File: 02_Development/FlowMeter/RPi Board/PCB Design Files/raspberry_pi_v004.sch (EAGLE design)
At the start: 116 parts, among them J5 POWER_JACK, P1 SPL006-007, P2 SPL006-007, P3 SPL006-007, P4 SPL006-007, P5 SPL006-007, Q1 4.3A/20V/54mΩ, Q2 500mA/300V, U6 TCA9548APWR, U7 TCA9548APWR

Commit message: updated PCB with new 5V regulator (#145)
* added new 5V regulator

added new 5V regulator as existing regulator was out-of-stock at JLCPCB

* updated capacitor

changed C22 and C25 to 1206 footprint and specified 2mohm low ESR cap
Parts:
- removed C13: 33n, SparkFun-Capacitors:CAP-0805
- removed C23: 1uF, SparkFun-Capacitors:CAP-0805
- removed D3: 3A/40V/500mV, SparkFun-DiscreteSemi:DIODE-SCHOTTKY-B340A
- removed L1: INDUCTOR12.5, th_libraries:INDUCTOR12.5
- removed R1: 10K, SparkFun-Resistors:0.3OHM-0805-1/8W-1%
- removed R2: 3.3K, SparkFun-Resistors:0.3OHM-0805-1/8W-1%
- removed VREG1: XL4015, th_libraries:XL4015
- added C24: 100nF, SparkFun-Capacitors:CAP-0805
- added C25: 22uF, microbuilder:CAP_CERAMIC_1206
- added C27: 10uF, microbuilder:CAP_CERAMIC0805-NOOUTLINE
- added C28: 470nF, SparkFun-Capacitors:CAP-0805
- added C29: 4.7pF, SparkFun-Capacitors:CAP-0603
- added INDUCT: INDUCTOR_6.6_7.3, th_libraries:INDUCTOR_6.6_7.3
- added R49: 365K, SparkFun-Passives:RESISTOR0805-RES
- added R50: 49.9K, SparkFun-Passives:RESISTOR0805-RES
- added R51: 100K, SparkFun-Passives:RESISTOR0805-RES
- added R52: 10K, SparkFun-Resistors:0.3OHM-0805-1/8W-1%
- added TPS: TPS56528, th_libraries:TPS56528
- C19: value 1uF -> 10uF; device SparkFun-Capacitors:CAP-0805 -> microbuilder:CAP_CERAMIC0805-NOOUTLINE
- C20: value 1uF -> 100nF
- C22: value 220uF -> 22uF; device SparkFun-Capacitors:560UF-PANASONIC_G-25V-20% -> microbuilder:CAP_CERAMIC_1206
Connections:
- new net N$14: C24.1, TPS.VBST
- new net N$17: R51.1, TPS.PG
- new net N$27: R52.2, TPS.EN
- net 12V: now also C21.+, C27.1, R52.1, TPS.VIN; no longer C22.+, VREG1.IN
- net 5V: now also C22.1, C25.1, C29.1, INDUCT.2, R49.2; no longer C13.1, C21.+, C23.1, L1.1, R1.1
- net GND: now also C19.2, C22.2, C25.2, C27.2, C28.2, R50.2, TPS.GND, TPS.PWPD; no longer C22.-, C23.2, D3.A, R2.2, VREG1.GND
- net N$11: now also C29.2, R49.1, R50.1, TPS.VFB; no longer C13.2, R1.2, R2.1, VREG1.FB
- net N$6: now also C24.2, INDUCT.1, TPS.SW; no longer D3.C, L1.2, VREG1.SW
- net N$7: now also C28.1, R51.2, TPS.VREG; no longer C19.2, VREG1.VC
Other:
- note added: "3.3uH"
- note added: "Regulator - TPS56528DDAR https://datasheet.lcsc.com/szlcsc/1805310826_Texas-Instruments-TPS56528DDAR_C138716.pdf LCSC Part# C138716 Package SOIC - 150mill grounding pad Input Capacitor 330uF, 35V (only 25V required) LCSC Part# C134522 https://datasheet.lcsc.com/szlcsc/Lelon-VZH331M1VTR-1010K_C134522.pdf 10X10MM ROHS, panasonic G Inductor 3.3uH, 6.5amps MHCI06030-3R3M-R8A - 6.6x7.3mm LCSC Part# C2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"
- note added: "version 004 12/5/2020 - add new 5V regulator version 003 - removed piezo buzzer - used transistor/P-ch mosfet for triggering sensirion power - added 33nF capacitor on the 5V power regulator based on rev1.6 of the data sheet"
- note removed: "Regulator - XL4015E1 https://lcsc.com/product-detail/DC-DC-Converters_XL4015E1_C51661.html/?href=jlc-SMT LCSC Part# C51661 Package TO-263-5 Input capacitor Spec - 50V Selection 220uF, 50V LCSC Part# C134732 https://datasheet.lcsc.com/szlcsc/Lelon-VE-221M1HTR-1010_C134732.pdf 10X10MM ROHS, panasonic G Output Capacitor 330uF, 35V (only 25V required) LCSC Part# C134522 https://datasheet.lcsc.com/szl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"
- note removed: "version 003 - removed piezo buzzer - used transistor/P-ch mosfet for triggering sensirion power - added 33nF capacitor on the 5V power regulator based on rev1.6 of the data sheet"
- moved on the sheet: C19, C20, C21

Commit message: Next revision of PCB
Changed I2C pullup resistors to 3Kohm

General tidy up and fix of issues on the PCB. Tweaked some polygons to eliminate sharp corners, made some traces larger.
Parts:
- R10, R13, R14, R15, R16, R17, R18, R29, R30, R31, R32, R33, R34, R35, R36, R7, R8, R9: value 10K -> 3K

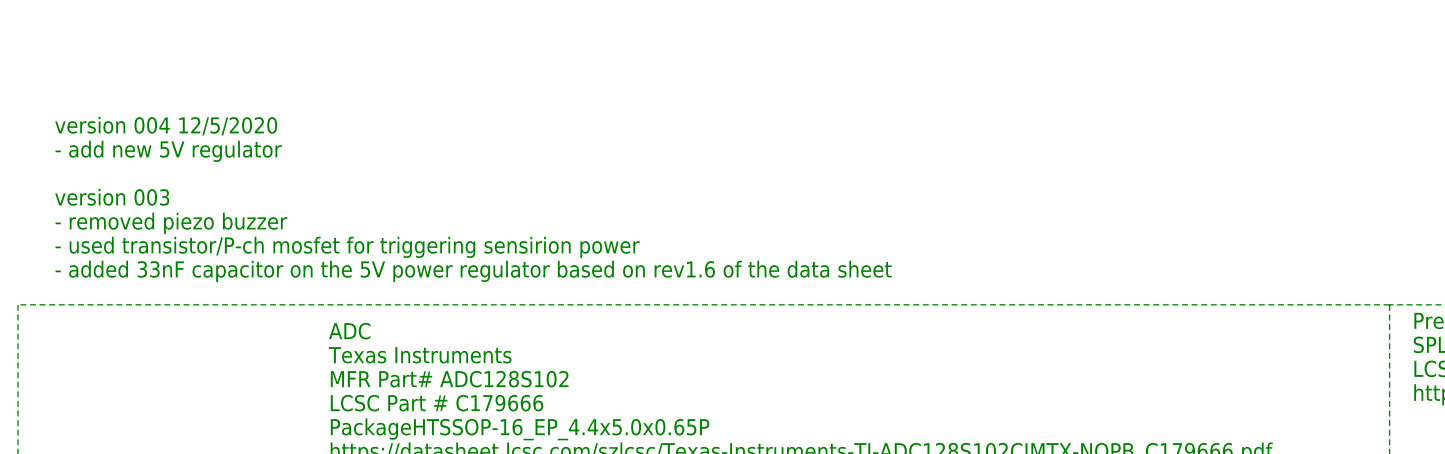
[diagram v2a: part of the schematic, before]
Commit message: Changes made as per PR152
Changes made as requested, I also updated the pdf of the schematic and the dru file.

One thing I have noticed is that generating the BOM automatically comes up with the incorrect resistor value of 0.3 Ohms. I suspect this is to do with the library that is being used.
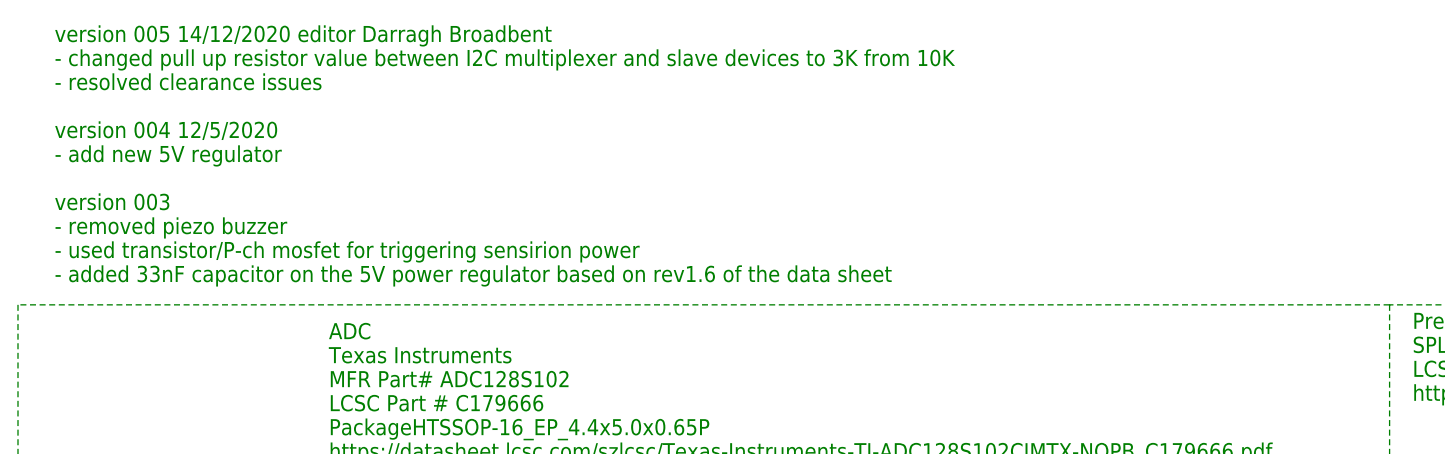
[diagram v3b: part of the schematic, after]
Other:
- note added: "version 005 14/12/2020 editor Darragh Broadbent - changed pull up resistor value between I2C multiplexer and slave devices to 3K from 10K - resolved clearance issues version 004 12/5/2020 - add new 5V regulator version 003 - removed piezo buzzer - used transistor/P-ch mosfet for triggering sensirion power - added 33nF capacitor on the 5V power regulator based on rev1.6 of the data sheet"
- note removed: "version 004 12/5/2020 - add new 5V regulator version 003 - removed piezo buzzer - used transistor/P-ch mosfet for triggering sensirion power - added 33nF capacitor on the 5V power regulator based on rev1.6 of the data sheet"
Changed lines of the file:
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@@
 - - 12VDC/5DC converter is active, jumper is made and RPI,Display, and peripherials powered by converter
 Scenario #4 - </text>
-<text x="-122.936" y="203.708" size="1.778" layer="91" align="top-left">version 004 12/5/2020
+<text x="-122.936" y="213.868" size="1.778" layer="91" align="top-left">version 005 14/12/2020 editor Darragh Broadbent
+- changed pull up resistor value between I2C multiplexer and slave devices to 3K from 10K
+- resolved clearance issues
+version 004 12/5/2020
 - add new 5V regulator
 version 003
